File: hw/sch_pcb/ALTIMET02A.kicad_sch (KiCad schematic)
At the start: 14 parts, among them IC1 MS561101BA03-50, J1 HEADER_2x03_PARALLEL, J2 HEADER_2x03, J3 HEADER_2x05_PARALLEL

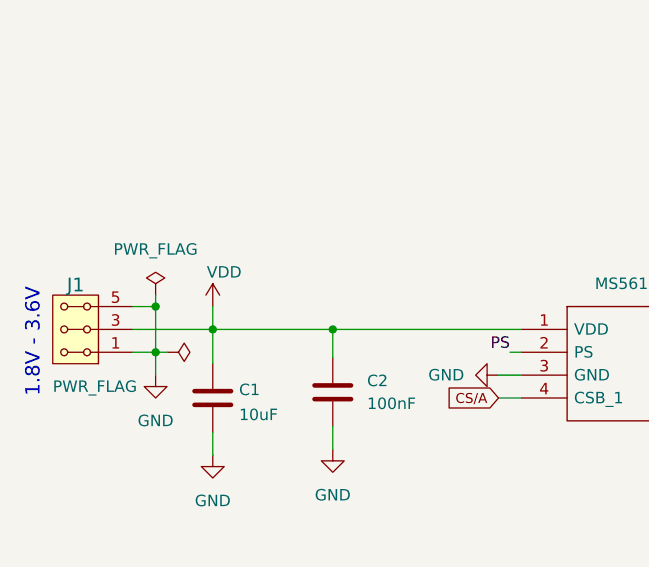
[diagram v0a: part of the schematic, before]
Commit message: Fix duplicate PWR_Flag Update symbols from libraries.
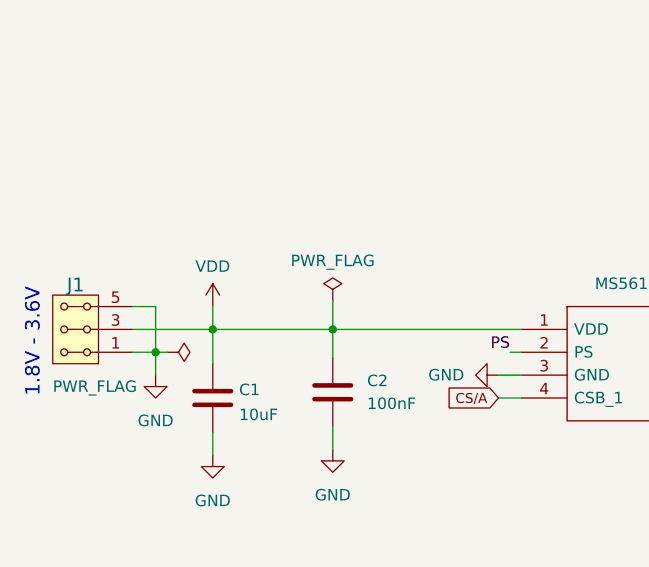
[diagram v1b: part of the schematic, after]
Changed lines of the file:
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@@
   (junction (at 92.71 78.74) (diameter 0) (color 0 0 0 0)
-  )
-  (junction (at 92.71 73.66) (diameter 0) (color 0 0 0 0)
   )
   (junction (at 248.92 134.62) (diameter 0) (color 0 0 0 0)
@@
     (stroke (width 0) (type default) (color 0 0 0 0))
   )
-  (wire (pts (xy 92.71 72.39) (xy 92.71 73.66))
-    (stroke (width 0) (type default) (color 0 0 0 0))
-  )
   (wire (pts (xy 261.62 34.29) (xy 261.62 36.83))
     (stroke (width 0) (type default) (color 0 0 0 0))
   )
   (wire (pts (xy 99.06 76.2) (xy 112.395 76.2))
+    (stroke (width 0) (type default) (color 0 0 0 0))
+  )
+  (wire (pts (xy 112.395 73.025) (xy 112.395 76.2))
     (stroke (width 0) (type default) (color 0 0 0 0))
   )
@@
     (pin "1")
   )
-  (symbol (lib_name "GND_3") (lib_id "power:GND") (at 99.06 90.17 0) (unit 1)
+  (symbol (lib_id "power:GND") (at 99.06 90.17 0) (unit 1)
     (in_bom yes) (on_board yes) (fields_autoplaced)
     (property "Reference" "#PWR03" (id 0) (at 99.06 96.52 0)
@@
     (pin "6")
   )
-  (symbol (lib_name "GND_2") (lib_id "power:GND") (at 92.71 81.28 0) (unit 1)
+  (symbol (lib_id "power:GND") (at 92.71 81.28 0) (unit 1)
     (in_bom yes) (on_board yes) (fields_autoplaced)
     (property "Reference" "#PWR01" (id 0) (at 92.71 87.63 0)
@@
     (pin "1")
   )
-  (symbol (lib_name "GND_3") (lib_id "power:GND") (at 112.395 89.535 0) (unit 1)
+  (symbol (lib_id "power:GND") (at 112.395 89.535 0) (unit 1)
     (in_bom yes) (on_board yes) (fields_autoplaced)
     (property "Reference" "#PWR04" (id 0) (at 112.395 95.885 0)
@@
   (symbol (lib_id "power:PWR_FLAG") (at 93.98 78.74 270) (unit 1)
     (in_bom yes) (on_board yes)
-    (property "Reference" "#FLG?" (id 0) (at 95.885 78.74 0)
+    (property "Reference" "#FLG02" (id 0) (at 95.885 78.74 0)
       (effects (font (size 1.27 1.27)) hide)
     )
@@
       (effects (font (size 1.27 1.27)) hide)
     )
-    (property "Value" "VDD" (id 1) (at 100.33 69.85 0))
+    (property "Value" "VDD" (id 1) (at 99.06 69.215 0))
     (property "Footprint" "" (id 2) (at 99.06 73.66 0)
       (effects (font (size 1.27 1.27)) hide)
@@
     (pin "1")
   )
-  (symbol (lib_id "power:PWR_FLAG") (at 92.71 72.39 0) (unit 1)
-    (in_bom yes) (on_board yes) (fields_autoplaced)
-    (property "Reference" "#FLG?" (id 0) (at 92.71 70.485 0)
-      (effects (font (size 1.27 1.27)) hide)
-    )
-    (property "Value" "PWR_FLAG" (id 1) (at 92.71 67.31 0))
-    (property "Footprint" "" (id 2) (at 92.71 72.39 0)
-      (effects (font (size 1.27 1.27)) hide)
-    )
-    (property "Datasheet" "~" (id 3) (at 92.71 72.39 0)
-      (effects (font (size 1.27 1.27)) hide)
-    )
-    (pin "1")
-  )
-  (symbol (lib_name "GND_1") (lib_id "power:GND") (at 130.81 81.28 270) (unit 1)
+  (symbol (lib_id "power:PWR_FLAG") (at 112.395 73.025 0) (unit 1)
+    (in_bom yes) (on_board yes)
+    (property "Reference" "#FLG01" (id 0) (at 112.395 71.12 0)
+      (effects (font (size 1.27 1.27)) hide)
+    )
+    (property "Value" "PWR_FLAG" (id 1) (at 112.395 68.58 0))
+    (property "Footprint" "" (id 2) (at 112.395 73.025 0)
+      (effects (font (size 1.27 1.27)) hide)
+    )
+    (property "Datasheet" "~" (id 3) (at 112.395 73.025 0)
+      (effects (font (size 1.27 1.27)) hide)
+    )
+    (pin "1")
+  )
+  (symbol (lib_id "power:GND") (at 130.81 81.28 270) (unit 1)
     (in_bom yes) (on_board yes) (fields_autoplaced)
     (property "Reference" "#PWR06" (id 0) (at 124.46 81.28 0)
@@
   )
   (symbol_instances
+    (path "/a563f1cc-3d38-409b-bcbf-a318ee494dca"
+      (reference "#FLG01") (unit 1) (value "PWR_FLAG") (footprint "")
+    )
     (path "/65dd51dc-dc3a-4aae-a001-2f0c32518331"
-      (reference "#FLG?") (unit 1) (value "PWR_FLAG") (footprint "")
-    )
-    (path "/a563f1cc-3d38-409b-bcbf-a318ee494dca"
-      (reference "#FLG?") (unit 1) (value "PWR_FLAG") (footprint "")
+      (reference "#FLG02") (unit 1) (value "PWR_FLAG") (footprint "")
     )
     (path "/3f4c1279-4303-49ec-92df-9b57c8acc5d7"

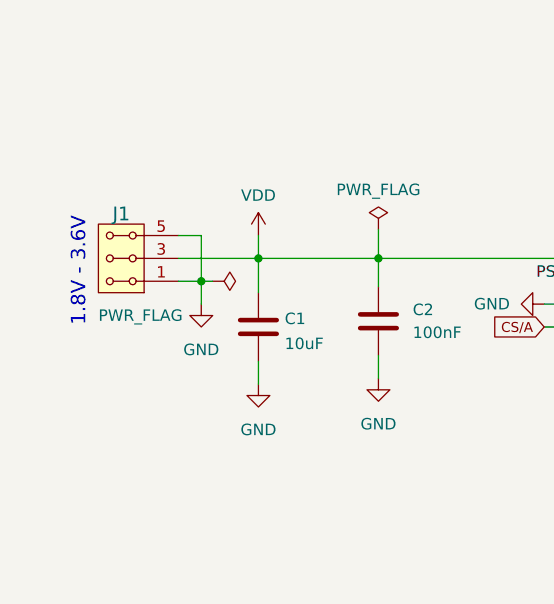
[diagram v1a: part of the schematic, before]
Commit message: power header deleted, i2c/spi solder jumper moved to the back side, i2c addr. added
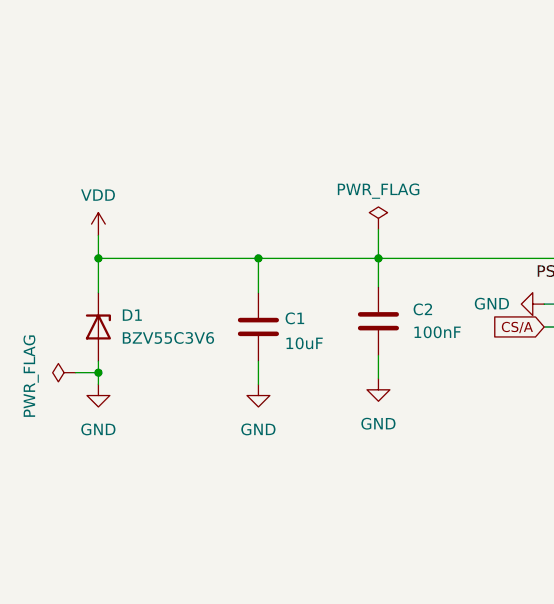
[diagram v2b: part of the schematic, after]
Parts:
- removed J1: HEADER_2x03_PARALLEL, Mlab_Pin_Headers:Straight_2x03, symbol MLAB_HEADER:HEADER_2x03_PARALLEL
- added D1: BZV55C3V6, Mlab_D:Diode-MiniMELF_Standard, symbol Device:D_Zener
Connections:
- net GND: now also D1.2 (A)
- net VDD: now also D1.1 (K)
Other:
- note removed: "1.8V - 3.6V"
